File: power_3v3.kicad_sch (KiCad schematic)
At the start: 21 parts, among them U12 TPS7A2033PDBVR, U7 TPS62913RPUR, U8 USBLC6-2SC6

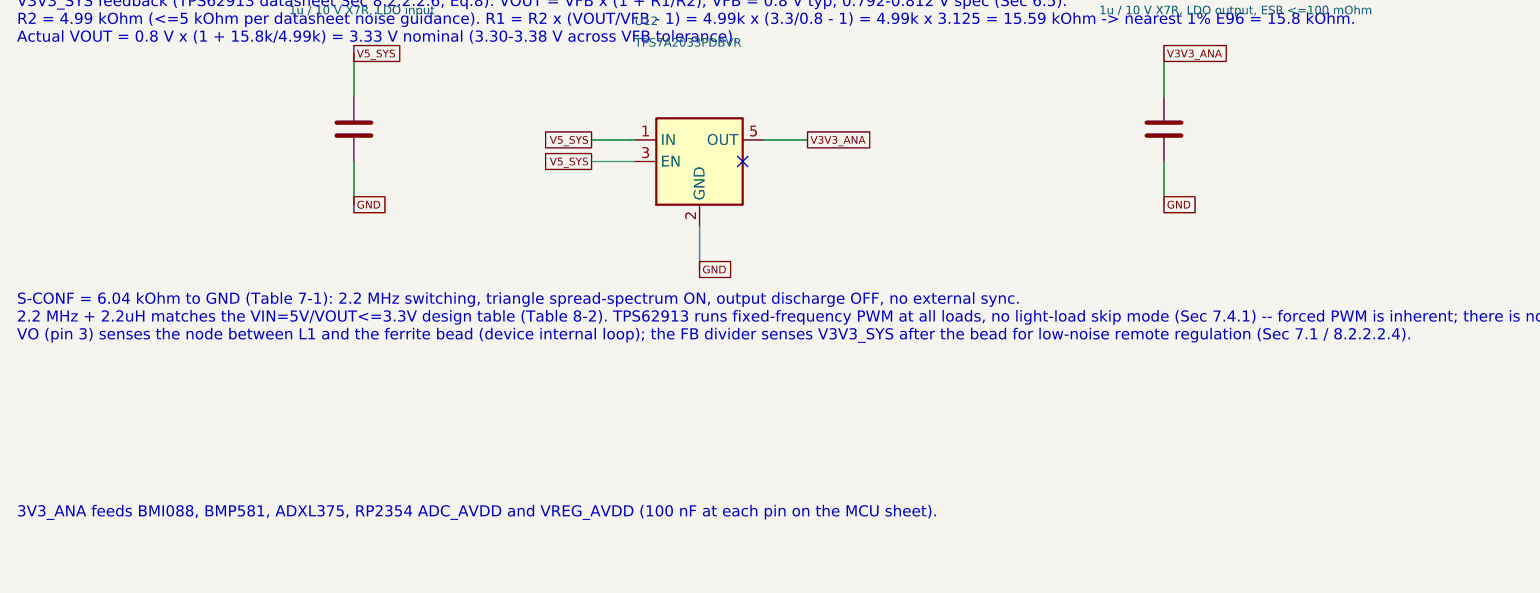
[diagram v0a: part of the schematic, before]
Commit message: Schematic review: TPS2121 input stage, DS-009 ports, sequencing and CS fixes; docs trimmed
Datasheet-grounded review of the full flight-controller schematic. Downstream
of the input everything verified pin-by-pin (TPS62913, TPS7A20, RP2354B,
BMI088/BMP581/ADXL375, W25Q128, microSD, PWM). The 5 V input stage did not:

- LM66100 (5.5 V rec-op / 6 V abs-max) replaced by one TPS2121 mux (U25):
  BEC priority on IN1, OV lockout ~5.86 V, current limit ~1.5 A, reverse
  blocking on both inputs, source status on GPIO39. Input spec 4.75-5.5 V.
- 5V_IN: 2x4.7 uF + 100 uF + SMAJ5.0A TVS; J3 JST-XH -> XT30PW-M (pin 1 GND).
- J6/J7/J9 reordered to Pixhawk DS-009 (VCC/sig/sig/GND); GPS/ELRS VCC 5 V.
- VIN_SENSE 22k/10k (full scale 10.6 V, was saturating at 5.5 V).
- TPS7A20 EN <- PWR_GOOD so V3V3_ANA rises after V3V3_SYS.
- RP2354B VREG_AVDD moved to V3V3_SYS (datasheet 6.1.8: must power up with
  VREG_VIN); ADC_AVDD stays on V3V3_ANA.
- 10k pull-ups on the four sensor chip-selects.
- ERC "global label appears once" re-enabled (0 hits).

Generator, netlist checker and SPICE decks updated (TPS2121 behavioral model,
new over-voltage and 2S mis-plug corners). Build idempotent, 143 pin mappings
PASS, ERC 0/0, all corners PASS.

Docs: POWER_*.md history removed, rationale folded into DESIGN_SPEC Decisions;
808 -> 290 lines across README, DESIGN_SPEC, LIBRARIES, simulations/README.

Co-Authored-By: Claude Fable 5.1 <noreply@anthropic.com>
Claude-Session: https://claude.ai/code/session_015cFNiWgf35VN2T43HaK8PE
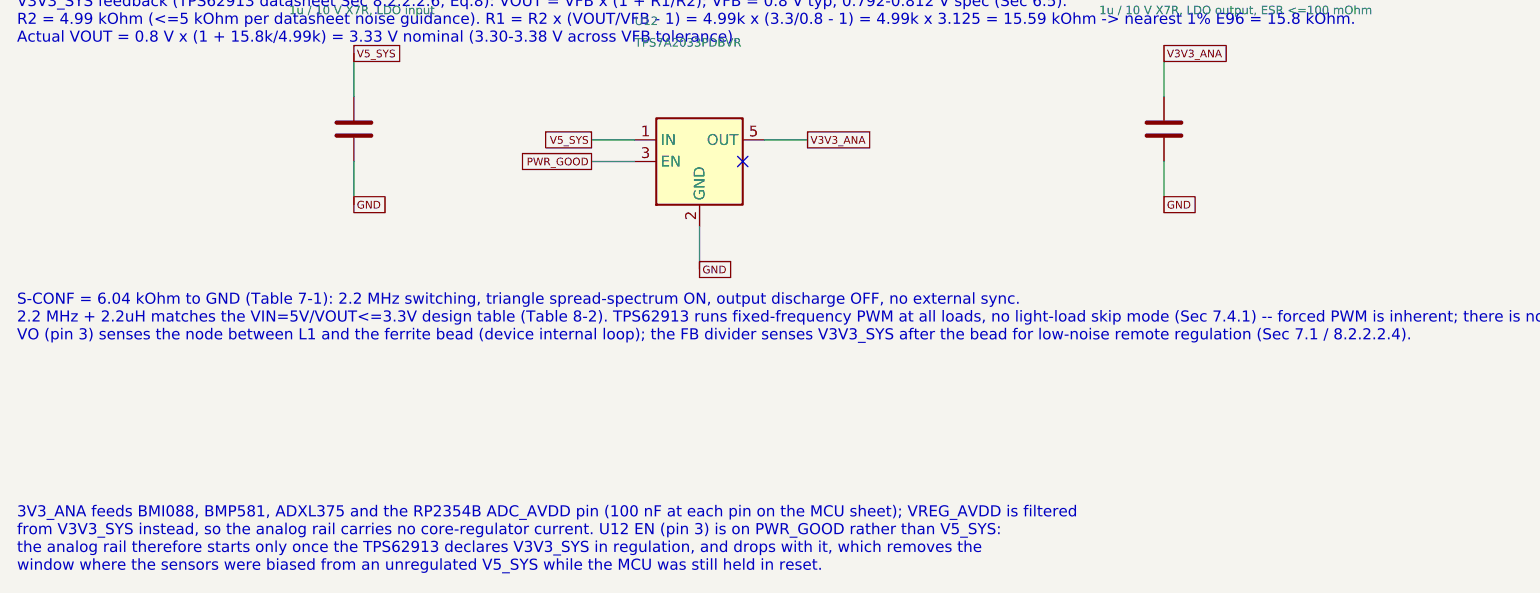
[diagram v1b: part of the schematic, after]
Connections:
- net PWR_GOOD: now also U12.3 (EN)
- net V5_SYS: no longer U12.3 (EN)
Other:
- note added: "3V3_ANA feeds BMI088, BMP581, ADXL375 and the RP2354B ADC_AVDD pin (100 nF at each pin on the MCU sheet); VREG_AVDD is filtered from V3V3_SYS instead, so the analog rail carries no core-regulator current. U12 EN (pin 3) is on PWR_GOOD rather than V5_SYS: the analog rail therefore starts only once the TPS62913 declares V3V3_SYS in regulation, and drops with it, which removes the window where the s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"
- note removed: "3V3_ANA feeds BMI088, BMP581, ADXL375, RP2354 ADC_AVDD and VREG_AVDD (100 nF at each pin on the MCU sheet)."

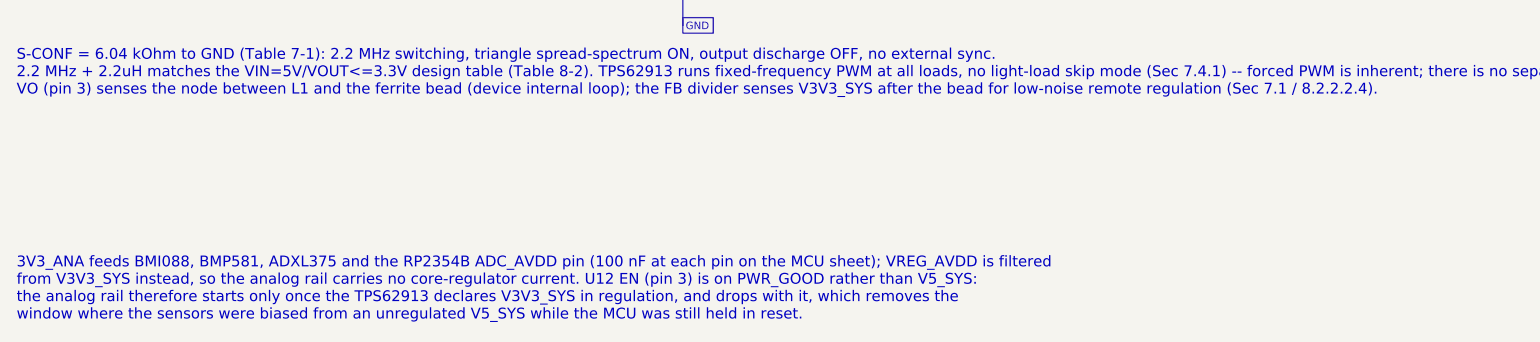
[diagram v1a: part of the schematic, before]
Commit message: Replace BMI088 with ICM-45686; vendor all footprints and 3D models for layout
Sensors: U21 is now the TDK ICM-45686 (single AP_CS on GPIO20 as IMU_CS,
INT1/INT2 on GPIO23/24, GPIO21 spare, R49 dropped, VDD+VDDIO on V3V3_ANA
with 100 nF + 1 uF each). Project-local symbol, footprint and stand-in STEP;
footprint numbering verified against DS-000577 Rev 1.0 Sec 11.2 (CCW, top
view). BMI088_SPI derived-symbol machinery removed from the generator.

Layout readiness: new tools/audit_footprints.py checks every component for
a resolvable footprint and present 3D model (128/128 OK). The seven official
KiCad footprints whose STEP files are absent from kicad-packages3d 10.0.6
are vendored into MARV_Packages.pretty with project-local models in
MARV_Packages.3dshapes: manufacturer STEPs (Coilcraft XGL4030, Molex
104031-0811), EasyEDA model (HRO TYPE-C-31-M-12), FreeCAD-generated bodies
from tools/3d/ (RP2354B QFN-80, TPS62913 RPU0010A, TPS2121 RUX0012A, Amass
XT30PW-M), and KiCad generic stand-ins (BMP581, ADXL375). Model offsets were
derived by measurement and confirmed in a rendered check board.
PROVENANCE.md records source, licence and SHA256 per model; LIBRARIES.md
lists the pre-fab 3D-viewer checks and the unverified dimensions.

Checks: build idempotent, ERC 0/0, check_power_netlist 149 mappings /
128 components, run_power_checks PASS, audit 0 needing action.

Co-Authored-By: Claude Fable 5.1 <noreply@anthropic.com>
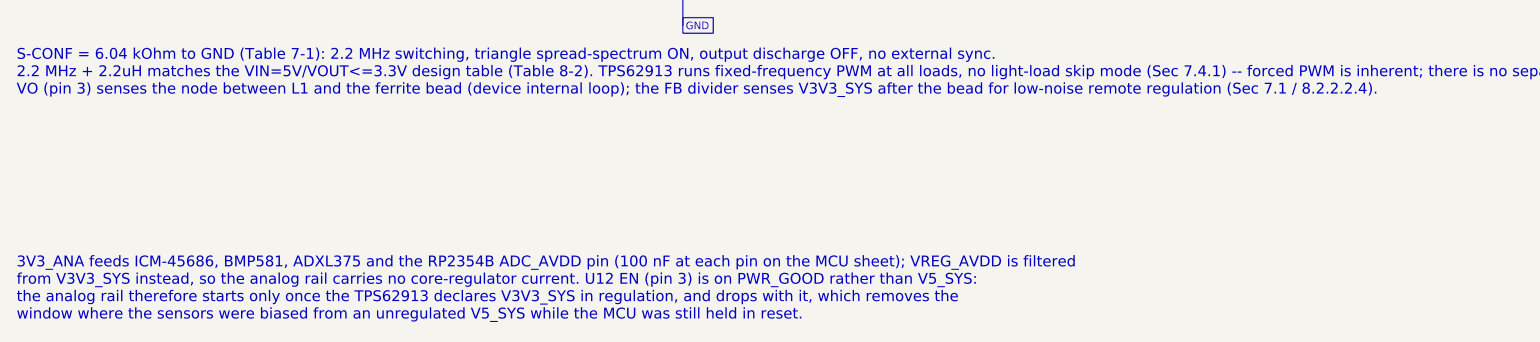
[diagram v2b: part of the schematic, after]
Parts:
- L2: footprint Inductor_SMD:L_Coilcraft_XxL4030 -> MARV_Packages:L_Coilcraft_XxL4030
- U7: footprint Package_DFN_QFN:Texas_RPU0010A_VQFN-HR-10_2x2mm_P0.5mm -> MARV_Packages:Texas_RPU0010A_VQFN-HR-10_2x2mm_P0.5mm
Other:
- note added: "3V3_ANA feeds ICM-45686, BMP581, ADXL375 and the RP2354B ADC_AVDD pin (100 nF at each pin on the MCU sheet); VREG_AVDD is filtered from V3V3_SYS instead, so the analog rail carries no core-regulator current. U12 EN (pin 3) is on PWR_GOOD rather than V5_SYS: the analog rail therefore starts only once the TPS62913 declares V3V3_SYS in regulation, and drops with it, which removes the window where th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"
- note removed: "3V3_ANA feeds BMI088, BMP581, ADXL375 and the RP2354B ADC_AVDD pin (100 nF at each pin on the MCU sheet); VREG_AVDD is filtered from V3V3_SYS instead, so the analog rail carries no core-regulator current. U12 EN (pin 3) is on PWR_GOOD rather than V5_SYS: the analog rail therefore starts only once the TPS62913 declares V3V3_SYS in regulation, and drops with it, which removes the window where the s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"

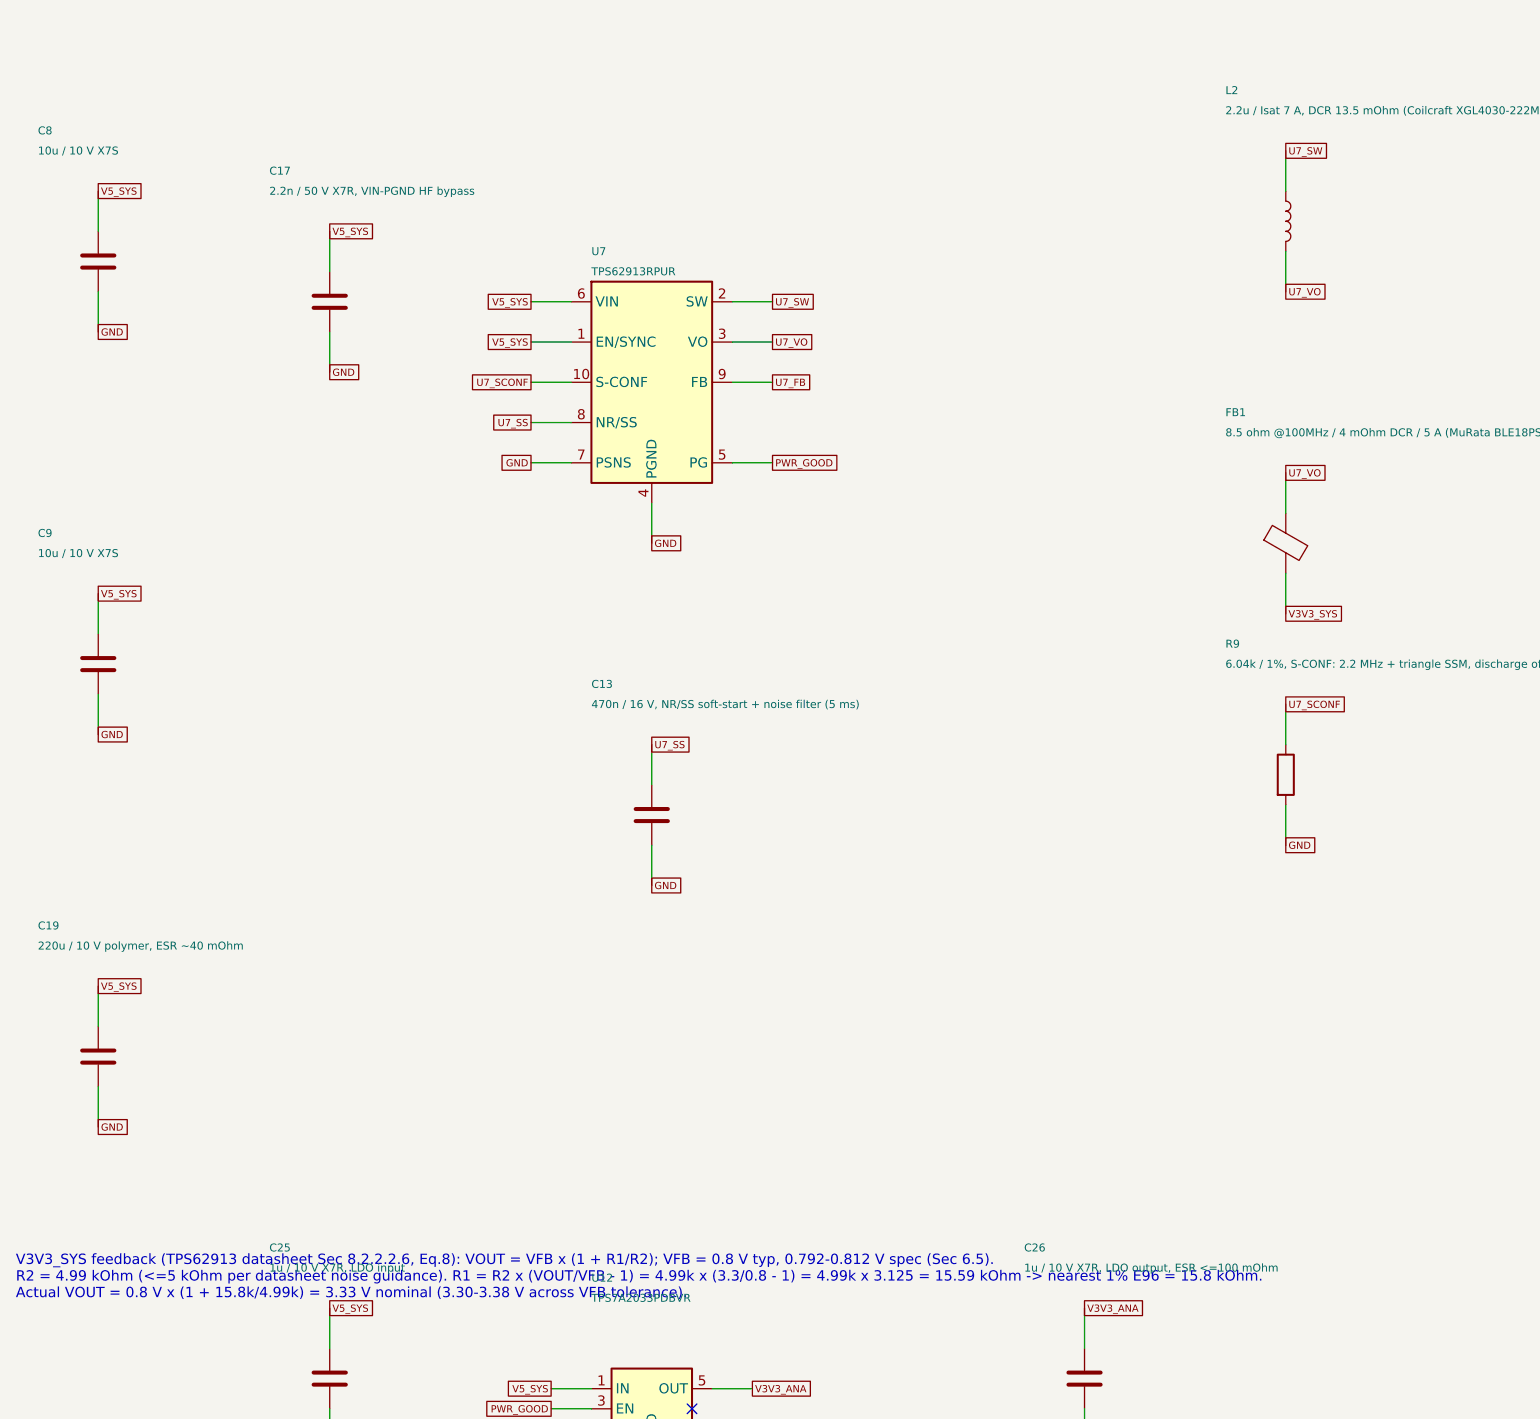
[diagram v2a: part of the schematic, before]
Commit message: Physical design: VBAT-in buck, ESC pad row, pad-row IO, 50 mm single-sided board
Power: the FC now takes raw 2-6S VBAT from the MicoAir AM32 4-in-1 ESC pad
row (CURR TX M4 M3 M2 M1 VBAT GND, J3) through an AP63205WU 5 V/2 A buck
(U26, XGL4030-472, 3 x 22 uF) into the existing TPS2121 mux; XT30 and its
TVS removed. VBAT sense 100k/10k (36 V FS) on ADC0, ESC current sense on
ADC2, ESC KISS telemetry on GPIO30.

IO per the physical spec (DESIGN_SPEC "Physical design"): solder pad rows
for GPS/ELRS/MAG (JST-GH removed), DBG and buzzer; 3x4 servo block for
PWM5-8; 2x6 spare-IO block; WS2812C-2020 RGB LED replaces the two discrete
LEDs; buzzer moved off-board to pads; flash socket is the 150-mil SOIC-8
(W25Q64 default, APS6404L PSRAM alternative); four 4.0 mm grommet holes on
the 30.5 mm pattern. Passives moved to 0402/0603 for the single-sided
envelope.

Board: tools/setup_pcb.py regenerates MARV-V2.kicad_pcb from the netlist —
50 x 50 mm, 4-layer JLC 7628 stack-up, net classes incl. a 90 ohm USB pair,
edge-anchored connectors, coarse interior placement, silk pad labels.
DRC leaves only unrouted items. The BMP581 project footprint had its 2-pad
edges at +/-0.5 mm (corner pads overlapped, three nets shorted); corrected
to Bosch Fig. 32 (+/-0.25 mm, 0.20 mm gaps).

Checks: ERC 0/0, 217 pin mappings / 139 components, run_power_checks PASS,
audit 139/139, pcb DRC unrouted-only.

Co-Authored-By: Claude Fable 5.1 <noreply@anthropic.com>
Claude-Session: https://claude.ai/code/session_01U6Ud7JA3CDTJZVcZZr5sx1
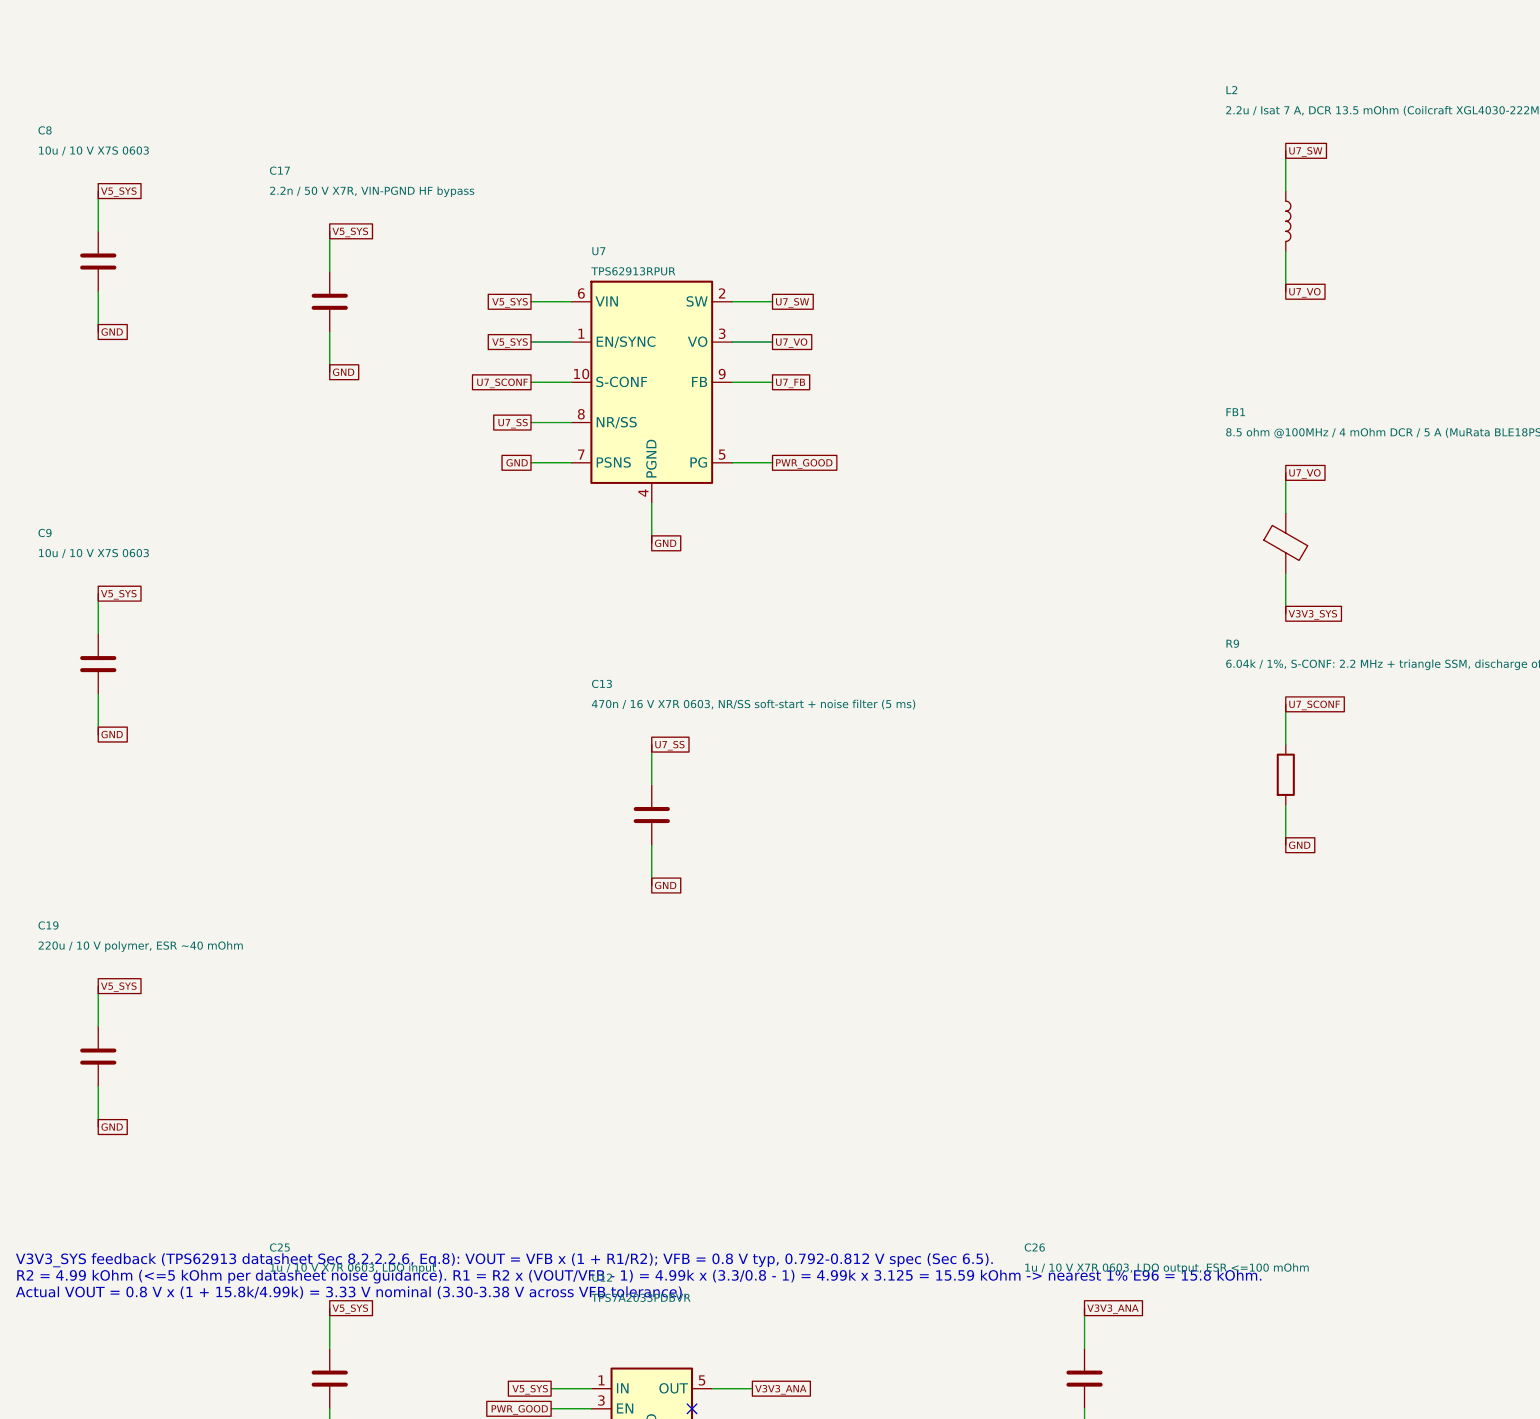
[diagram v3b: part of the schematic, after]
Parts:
- C13: value 470n / 16 V, NR/SS soft-start + noise filter (5 ms) -> 470n / 16 V X7R 0603, NR/SS soft-start + noise filter (5 ms); footprint Capacitor_SMD:C_0805_2012Metric -> Capacitor_SMD:C_0603_1608Metric
- C25: value 1u / 10 V X7R, LDO input -> 1u / 10 V X7R 0603, LDO input; footprint Capacitor_SMD:C_0805_2012Metric -> Capacitor_SMD:C_0603_1608Metric
- C26: value 1u / 10 V X7R, LDO output, ESR <=100 mOhm -> 1u / 10 V X7R 0603, LDO output, ESR <=100 mOhm; footprint Capacitor_SMD:C_0805_2012Metric -> Capacitor_SMD:C_0603_1608Metric
- C8, C9: value 10u / 10 V X7S -> 10u / 10 V X7S 0603; footprint Capacitor_SMD:C_0805_2012Metric -> Capacitor_SMD:C_0603_1608Metric
- R10, R7, R8, R9: footprint Resistor_SMD:R_0603_1608Metric -> Resistor_SMD:R_0402_1005Metric
